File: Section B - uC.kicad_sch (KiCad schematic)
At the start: 7 parts, among them J1 Conn_ARM_SWD_TagConnect_TC203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, U1 ATtiny204-SS

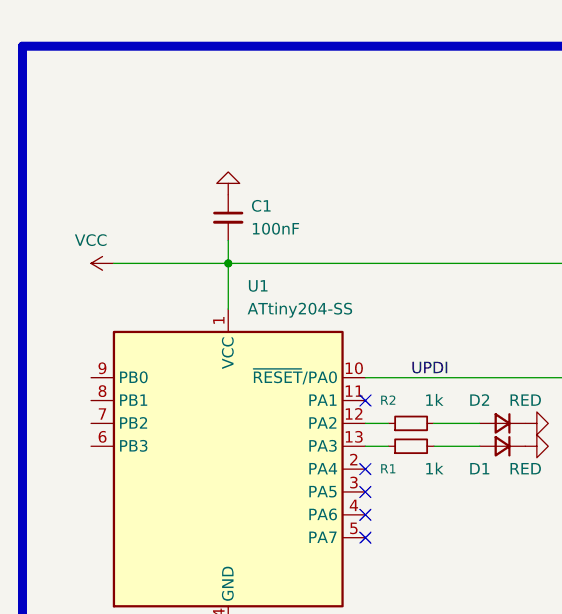
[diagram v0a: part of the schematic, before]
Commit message: schematic file names changed
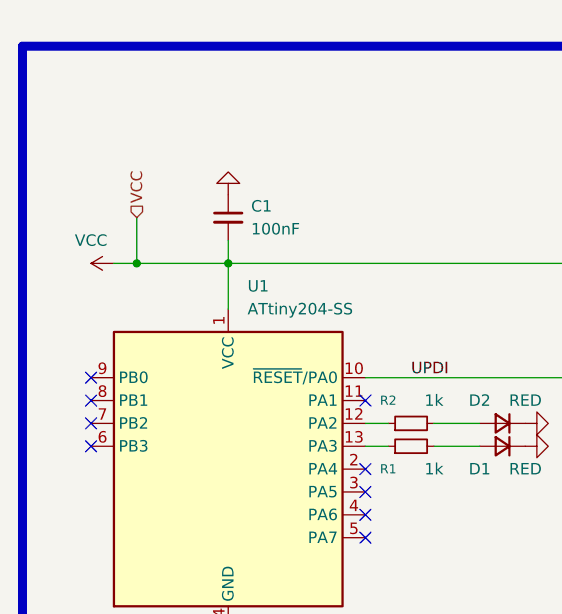
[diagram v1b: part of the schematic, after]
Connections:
- no-connect marks 8 -> 12
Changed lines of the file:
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@@
+	)
+	(junction
+		(at 58.42 63.5)
+		(diameter 0)
+		(color 0 0 0 0)
 	)
 	(junction
@@
 	)
 	(no_connect
+		(at 53.34 78.74)
+	)
+	(no_connect
+		(at 53.34 76.2)
+	)
+	(no_connect
+		(at 53.34 83.82)
+	)
+	(no_connect
 		(at 83.82 86.36)
 	)
@@
 	)
 	(no_connect
+		(at 53.34 81.28)
+	)
+	(no_connect
 		(at 121.92 66.04)
 	)
@@
 	(wire
 		(pts
+			(xy 58.42 63.5) (xy 68.58 63.5)
+		)
+		(stroke
+			(width 0)
+			(type default)
+		)
+	)
+	(wire
+		(pts
 			(xy 83.82 83.82) (xy 86.36 83.82)
 		)
@@
 	(wire
 		(pts
+			(xy 58.42 58.42) (xy 58.42 63.5)
+		)
+		(stroke
+			(width 0)
+			(type default)
+		)
+	)
+	(wire
+		(pts
 			(xy 68.58 63.5) (xy 109.22 63.5)
 		)
@@
 	(wire
 		(pts
-			(xy 55.88 63.5) (xy 68.58 63.5)
+			(xy 55.88 63.5) (xy 58.42 63.5)
 		)
 		(stroke
@@
 		)
 	)
+	(hierarchical_label "VCC"
+		(shape input)
+		(at 58.42 58.42 90)
+		(effects
+			(font
+				(size 1.27 1.27)
+			)
+			(justify left)
+		)
+	)

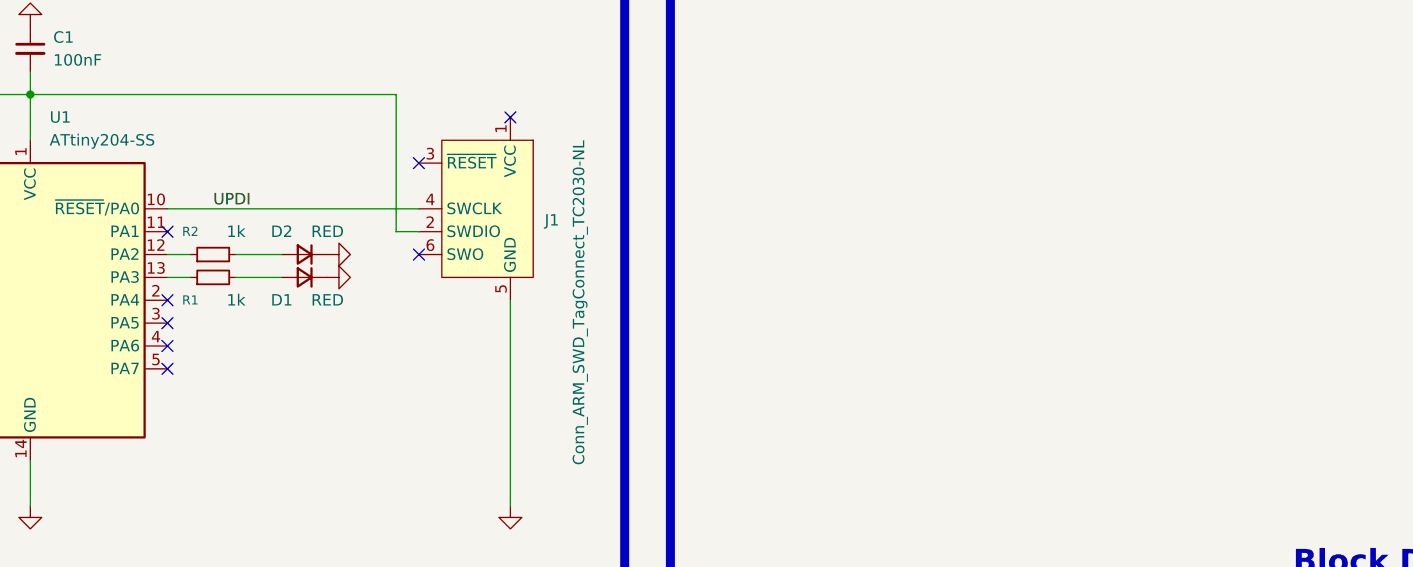
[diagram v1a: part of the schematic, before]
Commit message: sienkiewicz library missing value update
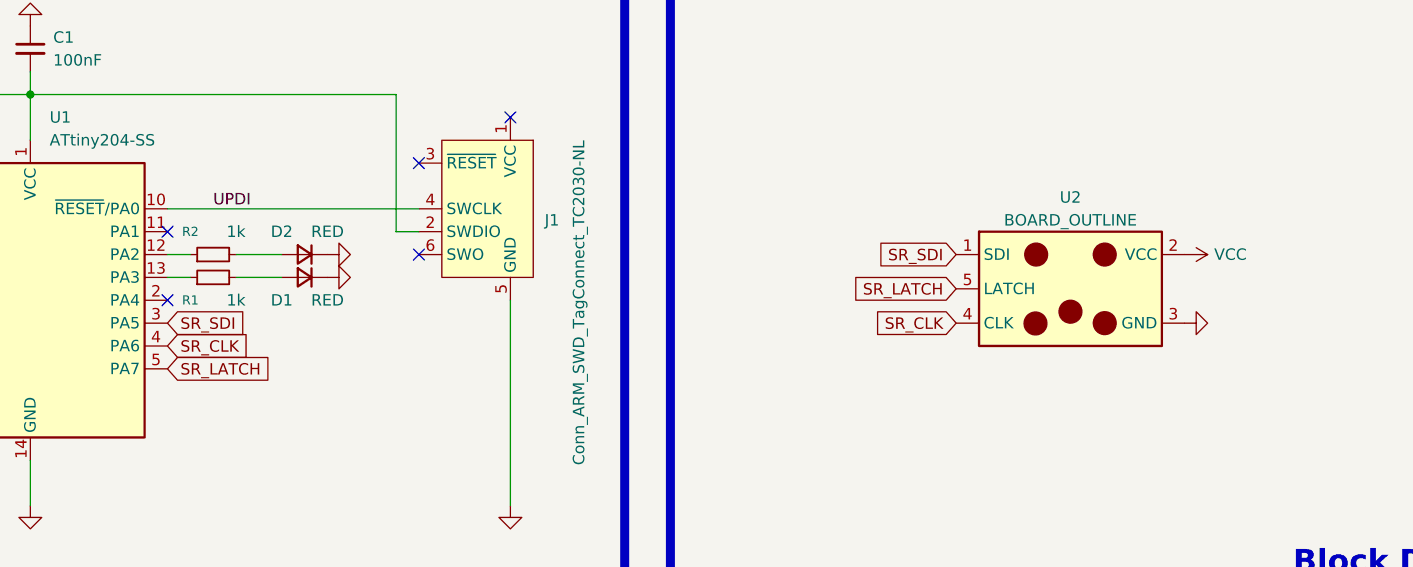
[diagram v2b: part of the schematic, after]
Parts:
- added U2: BOARD_OUTLINE, __Sienkiewicz:Sienkiewicz, symbol __Sienkiewicz:Sienkiewicz
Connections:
- net GND: now also U2.3 (GND)
- net VCC: now also U2.2 (VCC)
- net SR_SDI: now reaches U1.3 (PA5)
- net SR_SDI: now also U2.1 (SDI)
- net SR_CLK: now reaches U1.4 (PA6)
- net SR_CLK: now also U2.4 (CLK)
- net SR_LATCH: now reaches U1.5 (PA7)
- net SR_LATCH: now also U2.5 (LATCH)
- no-connect marks 12 -> 9

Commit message: board updatea
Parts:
- C1: footprint (none) -> Capacitor_SMD:C_1210_3225Metric
- D1, D2: footprint Diode_SMD:D_1206_3216Metric -> LED_SMD:LED_1206_3216Metric
- renumbered U2 to B1
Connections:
- net GND: now also R1.2, R2.2; no longer D1.1 (K), D2.1 (K)
- net SR_CLK: now also U1.6 (PB3); no longer U1.4 (PA6)
- net SR_LATCH: now also U1.7 (PB2); no longer U1.5 (PA7)
- net SR_SDI: now also U1.9 (PB0); no longer U1.3 (PA5)
- net at R2.1: now also D2.1 (K); no longer U1.13 (PA3)
- net at D2.2 (A): now also U1.12 (PA2); no longer R2.2
- net at R1.1: now also D1.1 (K); no longer U1.12 (PA2)
- net LED1: now reaches U1.8 (PB1)
- net LED1: now also D1.2 (A)
- new net TT: U1.5 (PA7)
- no-connect marks 9 -> 6
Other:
- moved on the sheet: B1, C1, D1, D2, J1, R1, R2

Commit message: pcb update
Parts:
- added TP1: GND, TestPoint:TestPoint_Pad_D1.5mm, symbol Connector:TestPoint
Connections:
- net GND: now also TP1.1
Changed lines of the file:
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@@
+	(wire
+		(pts
+			(xy 287.02 68.58) (xy 287.02 71.12)
+		)
+		(stroke
+			(width 0)
+			(type default)
+		)
+	)
 	(wire
 		(pts
@@
 	)
 	(symbol
+		(lib_id "power:GND")
+		(at 287.02 71.12 0)
+		(unit 1)
+		(exclude_from_sim no)
+		(in_bom yes)
+		(on_board yes)
+		(dnp no)
+		(fields_autoplaced yes)
+		(property "Reference" "#PWR015"
+			(at 287.02 77.47 0)
+			(effects
+				(font
+					(size 1.27 1.27)
+				)
+				(hide yes)
+			)
+		)
+		(property "Value" "GND"
+			(at 287.02 76.2 0)
+			(effects
+				(font
+					(size 1.27 1.27)
+				)
+				(hide yes)
+			)
+		)
+		(property "Footprint" ""
+			(at 287.02 71.12 0)
+			(effects
+				(font
+					(size 1.27 1.27)
+				)
+				(hide yes)
+			)
+		)
+		(property "Datasheet" ""
+			(at 287.02 71.12 0)
+			(effects
+				(font
+					(size 1.27 1.27)
+				)
+				(hide yes)
+			)
+		)
+		(property "Description" "Power symbol creates a global label with name \"GND\" , ground"
+			(at 287.02 71.12 0)
+			(effects
+				(font
+					(size 1.27 1.27)
+				)
+				(hide yes)
+			)
+		)
+		(pin "1"
+		)
+		(instances
+			(project "Sienkiewicz_TOUCH"
+				(path "/f9e05184-c88b-4a88-ae9c-ab2bdb32be7c/c5103ceb-5325-4a84-a025-9638a412984e/e744f3ce-03a6-44a6-8792-1447ef232b9a"
+					(reference "#PWR015")
+					(unit 1)
+				)
+			)
+		)
+	)
+	(symbol
 		(lib_id "Device:C_Small")
 		(at 68.58 63.5 0)
@@
 					(unit 1)
 				)
+			)
+		)
+	)
+	(symbol
+		(lib_id "Connector:TestPoint")
+		(at 287.02 68.58 0)
+		(unit 1)
+		(exclude_from_sim no)
+		(in_bom yes)
+		(on_board yes)
+		(dnp no)
+		(property "Reference" "TP1"
+			(at 287.02 60.96 0)
+			(effects
+				(font
+					(size 1.27 1.27)
+				)
+			)
+		)
+		(property "Value" "GND"
+			(at 287.02 63.5 0)
+			(effects
+				(font
+					(size 1.27 1.27)
+				)
+			)
+		)
+		(property "Footprint" "TestPoint:TestPoint_Pad_D1.5mm"
+			(at 292.1 68.58 0)
+			(effects
+				(font
+					(size 1.27 1.27)
+				)
+				(hide yes)
+			)
+		)
+		(property "Datasheet" "~"
+			(at 292.1 68.58 0)
+			(effects
+				(font
+					(size 1.27 1.27)
+				)
+				(hide yes)
+			)
+		)
+		(property "Description" "test point"
+			(at 287.02 68.58 0)
+			(effects
+				(font
+					(size 1.27 1.27)
+				)
+				(hide yes)
+			)
+		)
+		(pin "1"
+		)
+		(instances
+			(project ""
+				(path "/f9e05184-c88b-4a88-ae9c-ab2bdb32be7c/c5103ceb-5325-4a84-a025-9638a412984e/e744f3ce-03a6-44a6-8792-1447ef232b9a"
+					(reference "TP1")
+					(unit 1)
+				)

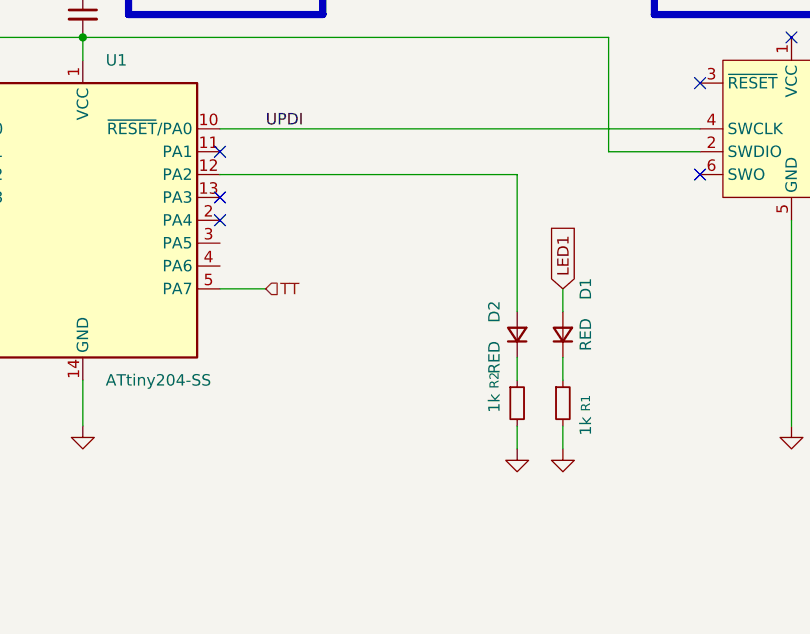
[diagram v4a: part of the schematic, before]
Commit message: led1,led2 better documented
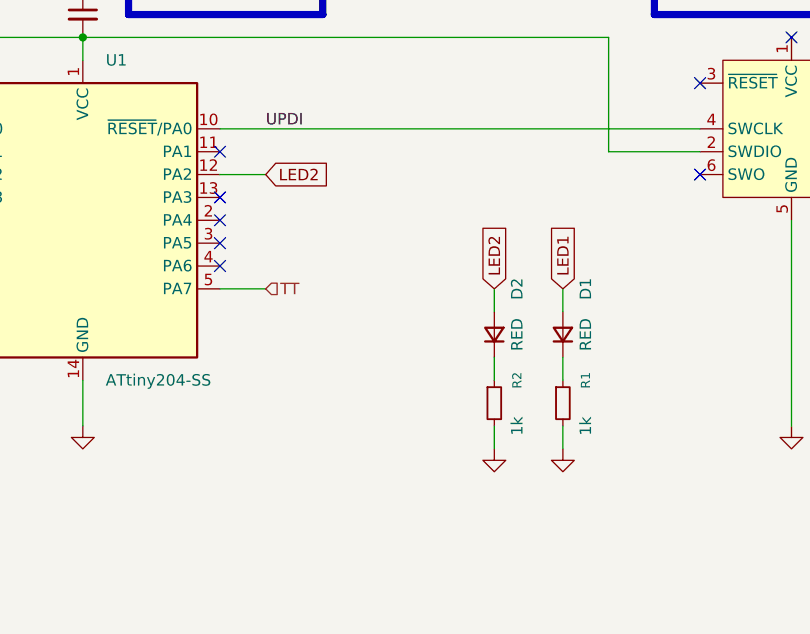
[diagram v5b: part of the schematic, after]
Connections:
- net LED2: now reaches D2.2 (A), U1.12 (PA2)
- no-connect marks 6 -> 8
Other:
- moved on the sheet: D2, R2
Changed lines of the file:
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@@
+	)
+	(no_connect
+		(at 83.82 88.9)
 	)
 	(no_connect
@@
 	)
 	(no_connect
+		(at 83.82 91.44)
+	)
+	(no_connect
 		(at 147.32 66.04)
 	)
@@
 	(wire
 		(pts
-			(xy 116.84 101.6) (xy 116.84 104.14)
+			(xy 114.3 101.6) (xy 114.3 104.14)
+		)
+		(stroke
+			(width 0)
+			(type default)
+		)
+	)
+	(wire
+		(pts
+			(xy 114.3 93.98) (xy 114.3 96.52)
 		)
 		(stroke
@@
 	(wire
 		(pts
-			(xy 116.84 109.22) (xy 116.84 111.76)
+			(xy 114.3 109.22) (xy 114.3 111.76)
+		)
+		(stroke
+			(width 0)
+			(type default)
+		)
+	)
+	(wire
+		(pts
+			(xy 88.9 81.28) (xy 83.82 81.28)
 		)
 		(stroke
@@
 	(wire
 		(pts
-			(xy 83.82 81.28) (xy 116.84 81.28)
-		)
-		(stroke
-			(width 0)
-			(type default)
-		)
-	)
-	(wire
-		(pts
 			(xy 53.34 66.04) (xy 68.58 66.04)
 		)
@@
 		(pts
 			(xy 127 66.04) (xy 127 78.74)
-		)
-		(stroke
-			(width 0)
-			(type default)
-		)
-	)
-	(wire
-		(pts
-			(xy 116.84 81.28) (xy 116.84 96.52)
 		)
 		(stroke
@@
 		)
 	)
+	(global_label "LED2"
+		(shape input)
+		(at 114.3 93.98 90)
+		(fields_autoplaced yes)
+		(effects
+			(font
+				(size 1.27 1.27)
+			)
+			(justify left)
+		)
+		(property "Intersheetrefs" "${INTERSHEET_REFS}"
+			(at 114.3 86.3382 90)
+			(effects
+				(font
+					(size 1.27 1.27)
+				)
+				(justify left)
+				(hide yes)
+			)
+		)
+	)
 	(global_label "SR_CLK"
 		(shape input)
@@
 		)
 	)
+	(global_label "LED2"
+		(shape input)
+		(at 88.9 81.28 0)
+		(fields_autoplaced yes)
+		(effects
+			(font
+				(size 1.27 1.27)
+			)
+			(justify left)
+		)
+		(property "Intersheetrefs" "${INTERSHEET_REFS}"
+			(at 96.5418 81.28 0)
+			(effects
+				(font
+					(size 1.27 1.27)
+				)
+				(justify left)
+				(hide yes)
+			)
+		)
+	)
 	(global_label "LED1"
 		(shape input)
@@
 	(symbol
 		(lib_id "Device:R_Small")
-		(at 116.84 106.68 0)
+		(at 114.3 106.68 0)
 		(unit 1)
 		(exclude_from_sim no)
@@
 		(dnp no)
 		(property "Reference" "R2"
-			(at 114.3 104.14 90)
+			(at 116.84 104.14 90)
 			(effects
 				(font
@@
 		)
 		(property "Value" "1k"
-			(at 114.3 106.68 90)
+			(at 116.84 109.22 90)
 			(effects
 				(font
@@
 		)
 		(property "Footprint" "Resistor_SMD:R_0805_2012Metric"
-			(at 116.84 106.68 0)
+			(at 114.3 106.68 0)
 			(effects
 				(font
@@
 		)
 		(property "Datasheet" "~"
-			(at 116.84 106.68 0)
+			(at 114.3 106.68 0)
 			(effects
 				(font
@@
 		)
 		(property "Description" "Resistor, small symbol"
-			(at 116.84 106.68 0)
+			(at 114.3 106.68 0)
 			(effects
 				(font
@@
 		(dnp no)
 		(property "Reference" "R1"
-			(at 124.46 106.68 90)
+			(at 124.46 104.14 90)
 			(effects
 				(font
@@
 	(symbol
 		(lib_id "Device:D_Small")
-		(at 116.84 99.06 90)
+		(at 114.3 99.06 90)
 		(unit 1)
 		(exclude_from_sim no)
@@
 		(dnp no)
 		(property "Reference" "D2"
-			(at 114.3 96.52 0)
+			(at 116.84 93.98 0)
 			(effects
 				(font
@@
 		)
 		(property "Value" "RED"
-			(at 114.3 101.6 0)
+			(at 116.84 99.06 0)
 			(effects
 				(font
@@
 		)
 		(property "Footprint" "LED_SMD:LED_1206_3216Metric"
-			(at 116.84 99.06 90)
+			(at 114.3 99.06 90)
 			(effects
 				(font
@@
 		)
 		(property "Datasheet" "~"
-			(at 116.84 99.06 90)
+			(at 114.3 99.06 90)
 			(effects
 				(font
@@
 		)
 		(property "Description" "Diode, small symbol"
-			(at 116.84 99.06 0)
+			(at 114.3 99.06 0)
 			(effects
 				(font
@@
 		)
 		(property "Sim.Device" "D"
-			(at 116.84 99.06 0)
+			(at 114.3 99.06 0)
 			(effects
 				(font
@@
 		)
 		(property "Sim.Pins" "1=K 2=A"
-			(at 116.84 99.06 0)
+			(at 114.3 99.06 0)
 			(effects
 				(font
@@
 	(symbol
 		(lib_id "power:GND")
-		(at 116.84 111.76 0)
+		(at 114.3 111.76 0)
 		(unit 1)
 		(exclude_from_sim no)
@@
 		(fields_autoplaced yes)
 		(property "Reference" "#PWR010"
-			(at 116.84 118.11 0)
+			(at 114.3 118.11 0)
 			(effects
 				(font
@@
 		)
 		(property "Value" "GND"
-			(at 116.84 116.84 0)
+			(at 114.3 116.84 0)
 			(effects
 				(font
@@
 		)
 		(property "Footprint" ""
-			(at 116.84 111.76 0)
+			(at 114.3 111.76 0)
 			(effects
 				(font
@@
 		)
 		(property "Datasheet" ""
-			(at 116.84 111.76 0)
+			(at 114.3 111.76 0)
 			(effects
 				(font
@@
 		)
 		(property "Description" "Power symbol creates a global label with name \"GND\" , ground"
-			(at 116.84 111.76 0)
-			(effects
-				(font
+			(at 114.3 111.76 0)
+			(effects
+				(font

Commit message: touch pad library creation
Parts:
- removed B1: BOARD_OUTLINE, __Sienkiewicz:Sienkiewicz, symbol __Sienkiewicz:Sienkiewicz
